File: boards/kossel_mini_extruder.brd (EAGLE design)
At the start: 57.7 x 50 mm, 20 parts

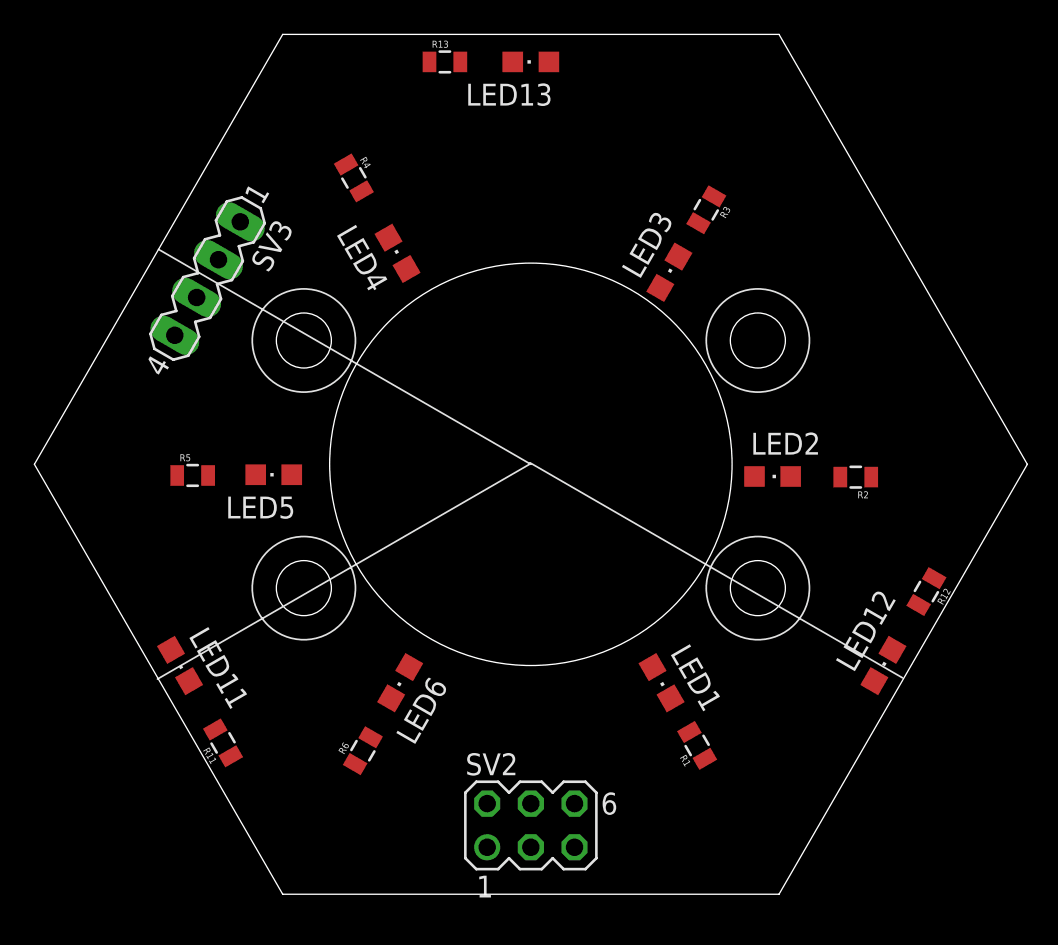
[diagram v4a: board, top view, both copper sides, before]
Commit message: first version of new extruder board
and golden dog fan mount
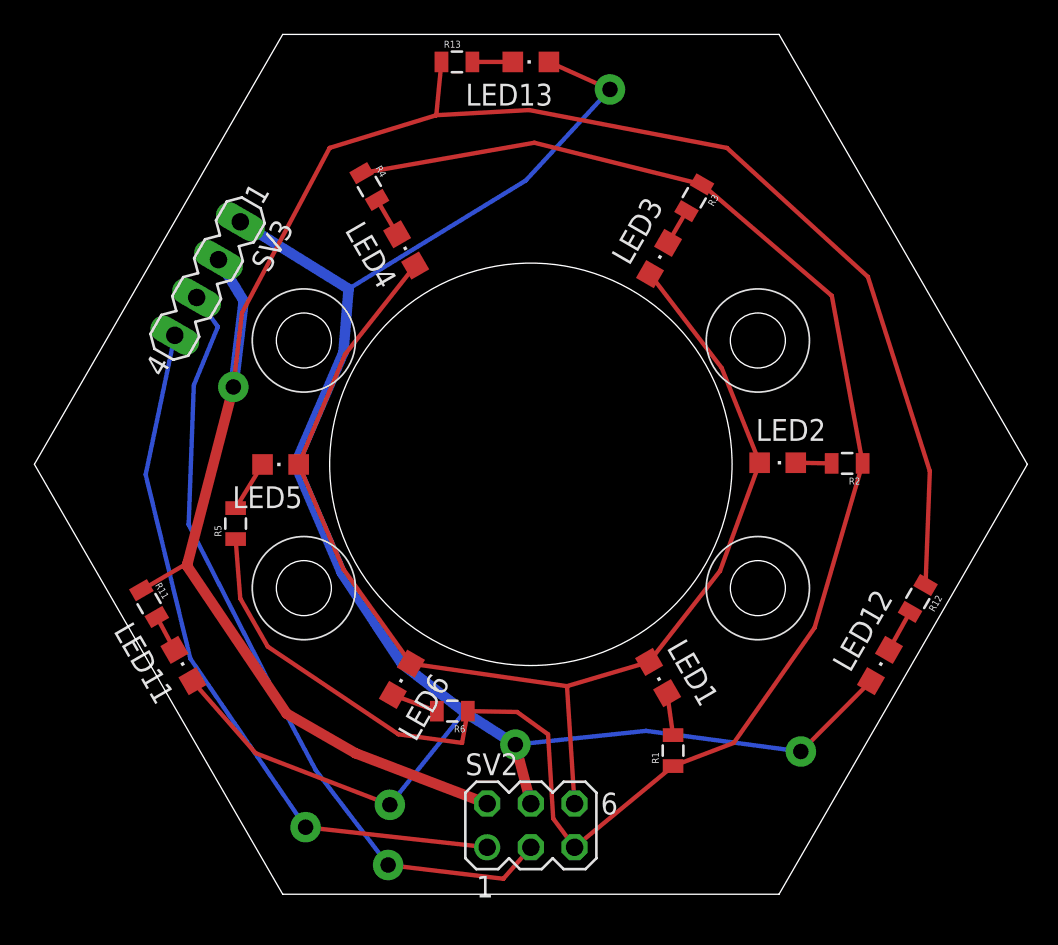
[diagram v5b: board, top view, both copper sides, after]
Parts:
- moved R11 9.17 mm to (7.80, 21.9), turned to 300 degrees
- moved R6 5.69 mm to (25.4, 15.6), turned to 180 degrees
- moved R5 3.75 mm to (12.8, 26.6), turned to 90 degrees
- moved R1 1.43 mm to (38.3, 13.4), turned to 90 degrees
- moved R4 1.03 mm to (20.6, 46.2)
- moved LED3 1.00 mm to (37.5, 42.0)
- moved R3 0.99 mm to (39.5, 45.5)
- moved R2 0.94 mm to (48.4, 30.1)
- moved LED2 0.85 mm to (44.4, 30.1)
- moved LED5 0.72 mm to (15.4, 30.0)
- moved R13 0.70 mm to (25.7, 53.4)
- moved R12 0.64 mm to (52.5, 22.2)
- moved LED4 0.54 mm to (22.7, 42.5)
- moved LED1 0.36 mm to (37.4, 17.6)
- moved LED6 0.22 mm to (22.5, 17.5)
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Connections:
- net GND: now also SV2.5; no longer SV2.4
- net HOT_12V: now also SV2.2, SV3.2; no longer SV2.5, SV3.1
- net HOT_SIG: now also SV2.4, SV3.1; no longer SV2.1, SV3.2
- net THERM_GND: now also SV2.1; no longer SV2.3
- net THERM_SIG: now also SV2.3; no longer SV2.2
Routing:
- net HOT_12V: track 0.00 -> 116.4 mm, vias 0 -> 1
- net HOT_SIG: track 0.00 -> 109.6 mm, vias 0 -> 4
- net GND: track 0.00 -> 103.0 mm
- net VCC: track 0.00 -> 74.1 mm
- net THERM_SIG: track 0.00 -> 46.1 mm, vias 0 -> 1
- net THERM_GND: track 0.00 -> 41.8 mm, vias 0 -> 1
- net N$5: track 0.00 -> 2.98 mm
- net N$6: track 0.00 -> 2.73 mm
- net N$17: track 0.00 -> 2.53 mm
- net N$1: track 0.00 -> 2.46 mm
- net N$18: track 0.00 -> 2.35 mm
- net N$4: track 0.00 -> 2.31 mm
- net N$16: track 0.00 -> 2.17 mm
- net N$3: track 0.00 -> 2.13 mm
- net N$2: track 0.00 -> 2.09 mm
